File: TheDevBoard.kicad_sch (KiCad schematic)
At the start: 0 parts

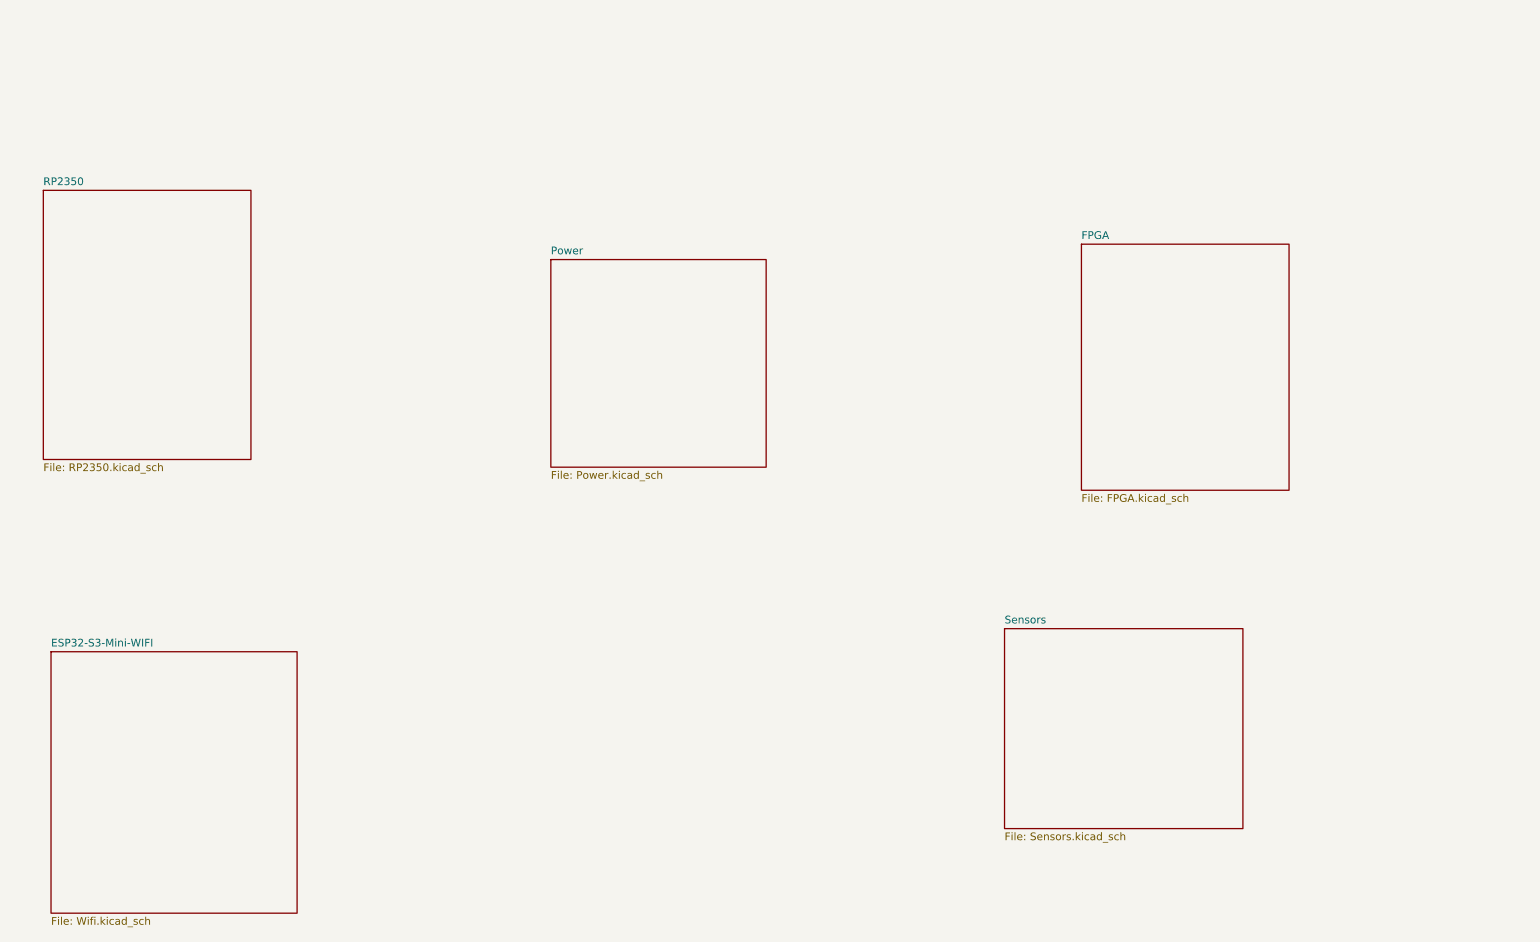
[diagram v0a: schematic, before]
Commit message: created esp32 s3 mini connection to rp2350 added SD card Routed them together
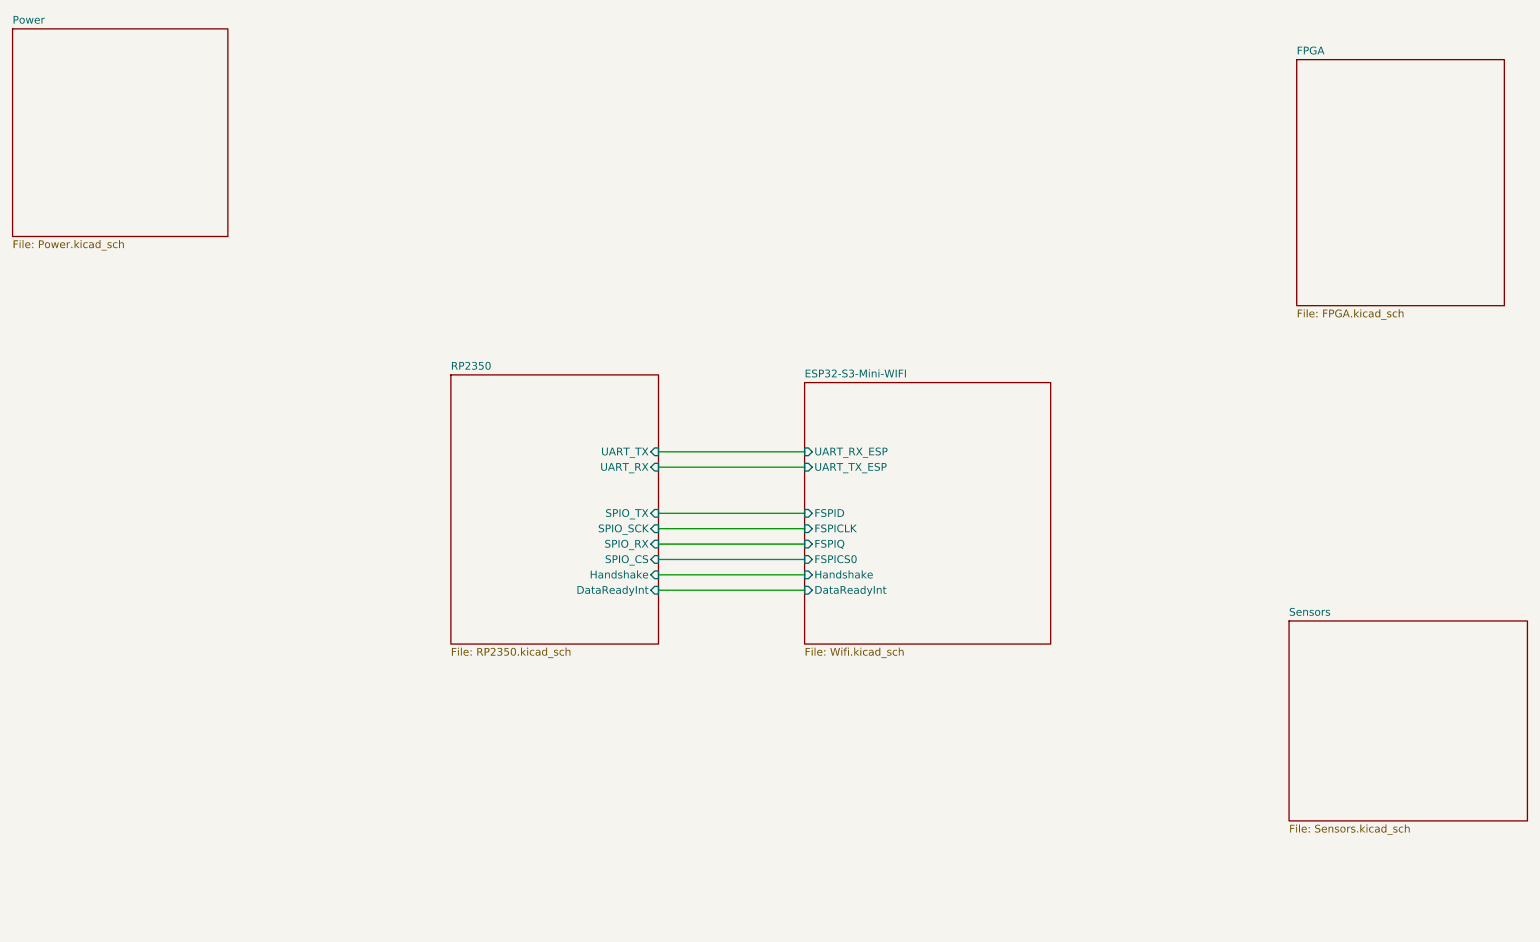
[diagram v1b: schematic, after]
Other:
- sheet ESP32-S3-Mini-WIFI ports: added DataReadyInt, FSPICLK, FSPICS0, FSPID, FSPIQ, Handshake, UART_RX_ESP, UART_TX_ESP; removed none
- sheet RP2350 ports: added DataReadyInt, Handshake, SPIO_CS, SPIO_RX, SPIO_SCK, SPIO_TX, UART_RX, UART_TX; removed none
